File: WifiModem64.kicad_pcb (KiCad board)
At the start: 2 copper layers, 55.9 x 59.7 mm, 39 parts, among them J1 C64-UserPort, J2 USB_B, Q1 BSS138, Q2 BSS138, Q3 BSS138, Q4 BSS138, SW1 Push, SW2 Reset, U1 WeMos_mini, U2 WeMos_D1_mini_OLED_Shield

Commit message: Added pull-down resistor on GPIO15 that is needed for internal flash boot.
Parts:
- added R9: 3k3, Resistors_SMD:R_0805_HandSoldering, B.Cu at (146.7, 108.6)
- moved REF** 1.91 mm to (147.3, 106.0)
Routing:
- net W_D8: track 51.7 -> 58.4 mm
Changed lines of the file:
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@@
 (kicad_pcb (version 4) (host pcbnew 4.0.7)
   (general
-    (links 86)
+    (links 88)
     (no_connects 0)
-    (area 118.644999 52.545 177.408 134.275001)
+    (area 118.669999 67.869999 174.700001 127.710001)
     (thickness 1.6)
     (drawings 47)
-    (tracks 272)
+    (tracks 276)
     (zones 0)
-    (modules 39)
+    (modules 40)
     (nets 39)
   )
@@
   )
   (module hackup:VIA-0.6mm (layer F.Cu)
-    (at 147.32 107.95)
+    (at 147.32 106.045)
     (fp_text reference REF** (at 0 1.2) (layer F.SilkS) hide
       (effects (font (size 1 1) (thickness 0.15)))
@@
     )
   )
+  (module Resistors_SMD:R_0805_HandSoldering (layer B.Cu)
+    (at 146.685 108.585 180)
+    (descr "Resistor SMD 0805, hand soldering")
+    (tags "resistor 0805")
+    (attr smd)
+    (fp_text reference R9 (at 0 1.7 180) (layer B.SilkS)
+      (effects (font (size 1 1) (thickness 0.15)) (justify mirror))
+    )
+    (fp_text value 3k3 (at 0 -1.75 180) (layer B.Fab)
+      (effects (font (size 1 1) (thickness 0.15)) (justify mirror))
+    )
+    (fp_text user %R (at 0 0 180) (layer B.Fab)
+      (effects (font (size 0.5 0.5) (thickness 0.075)) (justify mirror))
+    )
+    (fp_line (start -1 -0.62) (end -1 0.62) (layer B.Fab) (width 0.1))
+    (fp_line (start 1 -0.62) (end -1 -0.62) (layer B.Fab) (width 0.1))
+    (fp_line (start 1 0.62) (end 1 -0.62) (layer B.Fab) (width 0.1))
+    (fp_line (start -1 0.62) (end 1 0.62) (layer B.Fab) (width 0.1))
+    (fp_line (start 0.6 -0.88) (end -0.6 -0.88) (layer B.SilkS) (width 0.12))
+    (fp_line (start -0.6 0.88) (end 0.6 0.88) (layer B.SilkS) (width 0.12))
+    (fp_line (start -2.35 0.9) (end 2.35 0.9) (layer B.CrtYd) (width 0.05))
+    (fp_line (start -2.35 0.9) (end -2.35 -0.9) (layer B.CrtYd) (width 0.05))
+    (fp_line (start 2.35 -0.9) (end 2.35 0.9) (layer B.CrtYd) (width 0.05))
+    (fp_line (start 2.35 -0.9) (end -2.35 -0.9) (layer B.CrtYd) (width 0.05))
+    (pad 1 smd rect (at -1.35 0 180) (size 1.5 1.3) (layers B.Cu B.Paste B.Mask)
+      (net 25 GND))
+    (pad 2 smd rect (at 1.35 0 180) (size 1.5 1.3) (layers B.Cu B.Paste B.Mask)
+      (net 18 W_D8))
+    (model ${KISYS3DMOD}/Resistors_SMD.3dshapes/R_0805.wrl
+      (at (xyz 0 0 0))
+      (scale (xyz 1 1 1))
+      (rotate (xyz 0 0 0))
+    )
+  )
   (dimension 59.69 (width 0.3) (layer Dwgs.User)
     (gr_text "59.690 mm" (at 196.803 97.79 90) (layer Dwgs.User)
@@
   (segment (start 148.546411 99.015001) (end 170.859999 99.015001) (width 0.25) (layer F.Cu) (net 17))
   (segment (start 143.51 97.79) (end 147.32141 97.79) (width 0.25) (layer F.Cu) (net 17))
+  (segment (start 141.732 113.204) (end 142.632 113.204) (width 0.25) (layer B.Cu) (net 18))
+  (segment (start 142.632 113.204) (end 145.335 110.501) (width 0.25) (layer B.Cu) (net 18))
+  (segment (start 145.335 110.501) (end 145.335 109.485) (width 0.25) (layer B.Cu) (net 18))
+  (segment (start 145.335 109.485) (end 145.335 108.585) (width 0.25) (layer B.Cu) (net 18))
   (segment (start 141.732 113.204) (end 141.732 107.823) (width 0.25) (layer B.Cu) (net 18))
   (segment (start 141.732 107.823) (end 149.225 100.33) (width 0.25) (layer B.Cu) (net 18))

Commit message: Pull down resistor is not optional so it should be through hole.
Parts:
- R9: footprint Resistors_SMD:R_0805_HandSoldering -> Resistors_THT:R_Axial_DIN0207_L6.3mm_D2.5mm_P2.54mm_Vertical; moved to F.Cu
- moved R9 25.9 mm to (121.9, 116.2), turned to 90 degrees
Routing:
- net W_D8: track 58.4 -> 65.6 mm
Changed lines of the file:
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@@
     (thickness 1.6)
     (drawings 47)
-    (tracks 276)
+    (tracks 274)
     (zones 0)
     (modules 40)
@@
   )
   (layers
-    (0 F.Cu signal hide)
+    (0 F.Cu signal)
     (31 B.Cu signal)
     (32 B.Adhes user)
@@
     )
   )
-  (module Resistors_SMD:R_0805_HandSoldering (layer B.Cu)
-    (at 146.685 108.585 180)
-    (descr "Resistor SMD 0805, hand soldering")
-    (tags "resistor 0805")
-    (attr smd)
-    (fp_text reference R9 (at 0 1.7 180) (layer B.SilkS)
-      (effects (font (size 1 1) (thickness 0.15)) (justify mirror))
-    )
-    (fp_text value 3k3 (at 0 -1.75 180) (layer B.Fab)
-      (effects (font (size 1 1) (thickness 0.15)) (justify mirror))
-    )
-    (fp_text user %R (at 0 0 180) (layer B.Fab)
-      (effects (font (size 0.5 0.5) (thickness 0.075)) (justify mirror))
-    )
-    (fp_line (start -1 -0.62) (end -1 0.62) (layer B.Fab) (width 0.1))
-    (fp_line (start 1 -0.62) (end -1 -0.62) (layer B.Fab) (width 0.1))
-    (fp_line (start 1 0.62) (end 1 -0.62) (layer B.Fab) (width 0.1))
-    (fp_line (start -1 0.62) (end 1 0.62) (layer B.Fab) (width 0.1))
-    (fp_line (start 0.6 -0.88) (end -0.6 -0.88) (layer B.SilkS) (width 0.12))
-    (fp_line (start -0.6 0.88) (end 0.6 0.88) (layer B.SilkS) (width 0.12))
-    (fp_line (start -2.35 0.9) (end 2.35 0.9) (layer B.CrtYd) (width 0.05))
-    (fp_line (start -2.35 0.9) (end -2.35 -0.9) (layer B.CrtYd) (width 0.05))
-    (fp_line (start 2.35 -0.9) (end 2.35 0.9) (layer B.CrtYd) (width 0.05))
-    (fp_line (start 2.35 -0.9) (end -2.35 -0.9) (layer B.CrtYd) (width 0.05))
-    (pad 1 smd rect (at -1.35 0 180) (size 1.5 1.3) (layers B.Cu B.Paste B.Mask)
+  (module Resistors_THT:R_Axial_DIN0207_L6.3mm_D2.5mm_P2.54mm_Vertical (layer F.Cu)
+    (at 121.92 116.205 90)
+    (descr "Resistor, Axial_DIN0207 series, Axial, Vertical, pin pitch=2.54mm, 0.25W = 1/4W, length*diameter=6.3*2.5mm^2, http://cdn-reichelt.de/documents/datenblatt/B400/1_4W%23YAG.pdf")
+    (tags "Resistor Axial_DIN0207 series Axial Vertical pin pitch 2.54mm 0.25W = 1/4W length 6.3mm diameter 2.5mm")
+    (fp_text reference R9 (at 1.27 -2.31 90) (layer F.SilkS)
+      (effects (font (size 1 1) (thickness 0.15)))
+    )
+    (fp_text value 3k3 (at 1.27 2.31 90) (layer F.Fab)
+      (effects (font (size 1 1) (thickness 0.15)))
+    )
+    (fp_circle (center 0 0) (end 1.25 0) (layer F.Fab) (width 0.1))
+    (fp_circle (center 0 0) (end 1.31 0) (layer F.SilkS) (width 0.12))
+    (fp_line (start 0 0) (end 2.54 0) (layer F.Fab) (width 0.1))
+    (fp_line (start 1.31 0) (end 1.44 0) (layer F.SilkS) (width 0.12))
+    (fp_line (start -1.6 -1.6) (end -1.6 1.6) (layer F.CrtYd) (width 0.05))
+    (fp_line (start -1.6 1.6) (end 3.65 1.6) (layer F.CrtYd) (width 0.05))
+    (fp_line (start 3.65 1.6) (end 3.65 -1.6) (layer F.CrtYd) (width 0.05))
+    (fp_line (start 3.65 -1.6) (end -1.6 -1.6) (layer F.CrtYd) (width 0.05))
+    (pad 1 thru_hole circle (at 0 0 90) (size 1.6 1.6) (drill 0.8) (layers *.Cu *.Mask)
       (net 25 GND))
-    (pad 2 smd rect (at 1.35 0 180) (size 1.5 1.3) (layers B.Cu B.Paste B.Mask)
+    (pad 2 thru_hole oval (at 2.54 0 90) (size 1.6 1.6) (drill 0.8) (layers *.Cu *.Mask)
       (net 18 W_D8))
-    (model ${KISYS3DMOD}/Resistors_SMD.3dshapes/R_0805.wrl
-      (at (xyz 0 0 0))
-      (scale (xyz 1 1 1))
+    (model ${KISYS3DMOD}/Resistors_THT.3dshapes/R_Axial_DIN0207_L6.3mm_D2.5mm_P2.54mm_Vertical.wrl
+      (at (xyz 0 0 0))
+      (scale (xyz 0.393701 0.393701 0.393701))
       (rotate (xyz 0 0 0))
     )
@@
   (segment (start 148.546411 99.015001) (end 170.859999 99.015001) (width 0.25) (layer F.Cu) (net 17))
   (segment (start 143.51 97.79) (end 147.32141 97.79) (width 0.25) (layer F.Cu) (net 17))
-  (segment (start 141.732 113.204) (end 142.632 113.204) (width 0.25) (layer B.Cu) (net 18))
-  (segment (start 142.632 113.204) (end 145.335 110.501) (width 0.25) (layer B.Cu) (net 18))
-  (segment (start 145.335 110.501) (end 145.335 109.485) (width 0.25) (layer B.Cu) (net 18))
-  (segment (start 145.335 109.485) (end 145.335 108.585) (width 0.25) (layer B.Cu) (net 18))
+  (segment (start 120.65 100.33) (end 121.92 101.6) (width 0.25) (layer B.Cu) (net 18))
+  (segment (start 121.92 101.6) (end 121.92 113.665) (width 0.25) (layer B.Cu) (net 18))
   (segment (start 141.732 113.204) (end 141.732 107.823) (width 0.25) (layer B.Cu) (net 18))
   (segment (start 141.732 107.823) (end 149.225 100.33) (width 0.25) (layer B.Cu) (net 18))

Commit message: Upgraded project files, modfied resistor footprint.
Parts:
- R9: footprint Resistors_THT:R_Axial_DIN0207_L6.3mm_D2.5mm_P2.54mm_Vertical -> Resistors_THT:R_Axial_DIN0207_L6.3mm_D2.5mm_P7.62mm_Horizontal
- moved R9 1.42 mm to (123.2, 115.6)
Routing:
- net W_D8: track 65.6 -> 60.4 mm
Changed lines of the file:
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@@
-(kicad_pcb (version 4) (host pcbnew 4.0.7)
+(kicad_pcb (version 20171130) (host pcbnew "(2017-12-18 revision 3c6d17026)-makepkg")
   (general
-    (links 88)
-    (no_connects 0)
-    (area 118.669999 67.869999 174.700001 127.710001)
     (thickness 1.6)
     (drawings 47)
@@
     (aux_axis_origin 118.745 67.945)
     (grid_origin 118.745 67.945)
-    (visible_elements 7FFEFFFF)
+    (visible_elements 7FFFFFFF)
     (pcbplotparams
       (layerselection 0x010f0_80000001)
       (usegerberextensions true)
+      (usegerberattributes false)
+      (usegerberadvancedattributes false)
+      (creategerberjobfile false)
       (excludeedgelayer true)
       (linewidth 0.100000)
@@
       (hpglpenspeed 20)
       (hpglpendiameter 15)
-      (hpglpenoverlay 2)
       (psnegative false)
       (psa4output false)
@@
       (effects (font (size 1 1) (thickness 0.15)) (justify mirror))
     )
-    (fp_text user %R (at 0 0 360) (layer B.Fab)
+    (fp_text user %R (at 0 0) (layer B.Fab)
       (effects (font (size 0.5 0.5) (thickness 0.075)) (justify mirror))
     )
@@
       (effects (font (size 1 1) (thickness 0.15)) (justify mirror))
     )
-    (fp_text user %R (at 0 0 360) (layer B.Fab)
+    (fp_text user %R (at 0 0) (layer B.Fab)
       (effects (font (size 0.5 0.5) (thickness 0.075)) (justify mirror))
     )
@@
       (effects (font (size 1 1) (thickness 0.15)) (justify mirror))
     )
-    (fp_text user %R (at 0 0 360) (layer B.Fab)
+    (fp_text user %R (at 0 0) (layer B.Fab)
       (effects (font (size 0.5 0.5) (thickness 0.075)) (justify mirror))
     )
@@
       (effects (font (size 1 1) (thickness 0.15)) (justify mirror))
     )
-    (fp_text user %R (at 0 0 360) (layer B.Fab)
+    (fp_text user %R (at 0 0) (layer B.Fab)
       (effects (font (size 0.5 0.5) (thickness 0.075)) (justify mirror))
     )
@@
     (tags "solder bridge")
     (attr smd)
-    (fp_text reference JP1 (at -1.778 -0.0635 450) (layer B.SilkS)
-      (effects (font (size 1 1) (thickness 0.15)) (justify mirror))
-    )
-    (fp_text value PwrSafety (at -1.8 0 450) (layer B.Fab)
+    (fp_text reference JP1 (at -1.778 -0.0635 90) (layer B.SilkS)
+      (effects (font (size 1 1) (thickness 0.15)) (justify mirror))
+    )
+    (fp_text value PwrSafety (at -1.8 0 90) (layer B.Fab)
       (effects (font (size 1 1) (thickness 0.15)) (justify mirror))
     )
@@
     )
   )
-  (module Resistors_THT:R_Axial_DIN0207_L6.3mm_D2.5mm_P2.54mm_Vertical (layer F.Cu)
-    (at 121.92 116.205 90)
-    (descr "Resistor, Axial_DIN0207 series, Axial, Vertical, pin pitch=2.54mm, 0.25W = 1/4W, length*diameter=6.3*2.5mm^2, http://cdn-reichelt.de/documents/datenblatt/B400/1_4W%23YAG.pdf")
-    (tags "Resistor Axial_DIN0207 series Axial Vertical pin pitch 2.54mm 0.25W = 1/4W length 6.3mm diameter 2.5mm")
-    (fp_text reference R9 (at 1.27 -2.31 90) (layer F.SilkS)
-      (effects (font (size 1 1) (thickness 0.15)))
-    )
-    (fp_text value 3k3 (at 1.27 2.31 90) (layer F.Fab)
-      (effects (font (size 1 1) (thickness 0.15)))
-    )
-    (fp_circle (center 0 0) (end 1.25 0) (layer F.Fab) (width 0.1))
-    (fp_circle (center 0 0) (end 1.31 0) (layer F.SilkS) (width 0.12))
-    (fp_line (start 0 0) (end 2.54 0) (layer F.Fab) (width 0.1))
-    (fp_line (start 1.31 0) (end 1.44 0) (layer F.SilkS) (width 0.12))
-    (fp_line (start -1.6 -1.6) (end -1.6 1.6) (layer F.CrtYd) (width 0.05))
-    (fp_line (start -1.6 1.6) (end 3.65 1.6) (layer F.CrtYd) (width 0.05))
-    (fp_line (start 3.65 1.6) (end 3.65 -1.6) (layer F.CrtYd) (width 0.05))
-    (fp_line (start 3.65 -1.6) (end -1.6 -1.6) (layer F.CrtYd) (width 0.05))
+  (module Resistors_THT:R_Axial_DIN0207_L6.3mm_D2.5mm_P7.62mm_Horizontal (layer F.Cu)
+    (at 123.19 115.57 90)
+    (descr "Resistor, Axial_DIN0207 series, Axial, Horizontal, pin pitch=7.62mm, 0.25W = 1/4W, length*diameter=6.3*2.5mm^2, http://cdn-reichelt.de/documents/datenblatt/B400/1_4W%23YAG.pdf")
+    (tags "Resistor Axial_DIN0207 series Axial Horizontal pin pitch 7.62mm 0.25W = 1/4W length 6.3mm diameter 2.5mm")
+    (fp_text reference R9 (at 3.81 -2.31 90) (layer F.SilkS)
+      (effects (font (size 1 1) (thickness 0.15)))
+    )
+    (fp_text value 3k3 (at 3.81 2.31 90) (layer F.Fab)
+      (effects (font (size 1 1) (thickness 0.15)))
+    )
+    (fp_line (start 0.66 -1.25) (end 0.66 1.25) (layer F.Fab) (width 0.1))
+    (fp_line (start 0.66 1.25) (end 6.96 1.25) (layer F.Fab) (width 0.1))
+    (fp_line (start 6.96 1.25) (end 6.96 -1.25) (layer F.Fab) (width 0.1))
+    (fp_line (start 6.96 -1.25) (end 0.66 -1.25) (layer F.Fab) (width 0.1))
+    (fp_line (start 0 0) (end 0.66 0) (layer F.Fab) (width 0.1))
+    (fp_line (start 7.62 0) (end 6.96 0) (layer F.Fab) (width 0.1))
+    (fp_line (start 0.6 -0.98) (end 0.6 -1.31) (layer F.SilkS) (width 0.12))
+    (fp_line (start 0.6 -1.31) (end 7.02 -1.31) (layer F.SilkS) (width 0.12))
+    (fp_line (start 7.02 -1.31) (end 7.02 -0.98) (layer F.SilkS) (width 0.12))
+    (fp_line (start 0.6 0.98) (end 0.6 1.31) (layer F.SilkS) (width 0.12))
+    (fp_line (start 0.6 1.31) (end 7.02 1.31) (layer F.SilkS) (width 0.12))
+    (fp_line (start 7.02 1.31) (end 7.02 0.98) (layer F.SilkS) (width 0.12))
+    (fp_line (start -1.05 -1.6) (end -1.05 1.6) (layer F.CrtYd) (width 0.05))
+    (fp_line (start -1.05 1.6) (end 8.7 1.6) (layer F.CrtYd) (width 0.05))
+    (fp_line (start 8.7 1.6) (end 8.7 -1.6) (layer F.CrtYd) (width 0.05))
+    (fp_line (start 8.7 -1.6) (end -1.05 -1.6) (layer F.CrtYd) (width 0.05))
     (pad 1 thru_hole circle (at 0 0 90) (size 1.6 1.6) (drill 0.8) (layers *.Cu *.Mask)
       (net 25 GND))
-    (pad 2 thru_hole oval (at 2.54 0 90) (size 1.6 1.6) (drill 0.8) (layers *.Cu *.Mask)
+    (pad 2 thru_hole oval (at 7.62 0 90) (size 1.6 1.6) (drill 0.8) (layers *.Cu *.Mask)
       (net 18 W_D8))
-    (model ${KISYS3DMOD}/Resistors_THT.3dshapes/R_Axial_DIN0207_L6.3mm_D2.5mm_P2.54mm_Vertical.wrl
+    (model ${KISYS3DMOD}/Resistors_THT.3dshapes/R_Axial_DIN0207_L6.3mm_D2.5mm_P7.62mm_Horizontal.wrl
       (at (xyz 0 0 0))
       (scale (xyz 0.393701 0.393701 0.393701))
@@
   (segment (start 148.546411 99.015001) (end 170.859999 99.015001) (width 0.25) (layer F.Cu) (net 17))
   (segment (start 143.51 97.79) (end 147.32141 97.79) (width 0.25) (layer F.Cu) (net 17))
-  (segment (start 120.65 100.33) (end 121.92 101.6) (width 0.25) (layer B.Cu) (net 18))
-  (segment (start 121.92 101.6) (end 121.92 113.665) (width 0.25) (layer B.Cu) (net 18))
+  (segment (start 123.19 107.95) (end 123.19 102.87) (width 0.25) (layer B.Cu) (net 18))
+  (segment (start 123.19 102.87) (end 120.65 100.33) (width 0.25) (layer B.Cu) (net 18))
   (segment (start 141.732 113.204) (end 141.732 107.823) (width 0.25) (layer B.Cu) (net 18))
   (segment (start 141.732 107.823) (end 149.225 100.33) (width 0.25) (layer B.Cu) (net 18))

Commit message: Freed GPIO15 and fixed footprints.
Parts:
- removed R9: 3k3, Resistors_THT:R_Axial_DIN0207_L6.3mm_D2.5mm_P7.62mm_Horizontal
- D1: footprint Diodes_SMD:D_0805 -> Diodes_SMD:D_SOD-323_HandSoldering
- Q1, Q2, Q3, Q4: footprint TO_SOT_Packages_SMD:SOT-23 -> TO_SOT_Packages_SMD:SOT-23_Handsoldering
- moved Q4 0.89 mm to (166.9, 108.5)
- moved Q1 0.89 mm to (158.6, 113.2)
- moved Q2 0.89 mm to (138.9, 113.2)
- moved Q3 0.89 mm to (130.7, 108.5)
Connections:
- JP3 pad 2: W_D8 -> W_D7
- Q2 pad 3: W_D8 -> W_D7
- R6 pad 2: W_D8 -> W_D7
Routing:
- net W_D8: track 60.4 -> 29.6 mm
- net W_D7: track 29.6 -> 55.7 mm
- net +3V3: track 99.9 -> 102.0 mm
- net RTS: track 12.0 -> 13.6 mm
- net W_D6: track 56.6 -> 58.1 mm
- net W_RX: track 60.8 -> 62.3 mm
- net W_TX: track 60.4 -> 61.9 mm
- net SP2: track 43.9 -> 45.4 mm
- net CTS: track 11.8 -> 13.2 mm
- net SP1: track 47.9 -> 49.3 mm

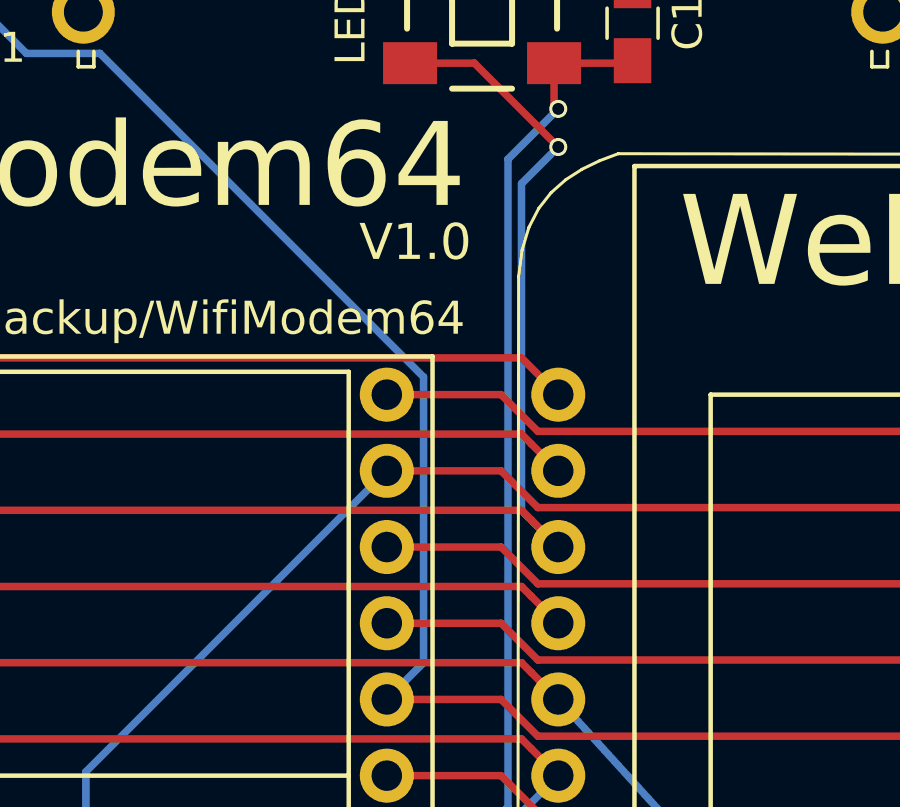
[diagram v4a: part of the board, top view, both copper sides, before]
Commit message: WS2812b not working on D0.
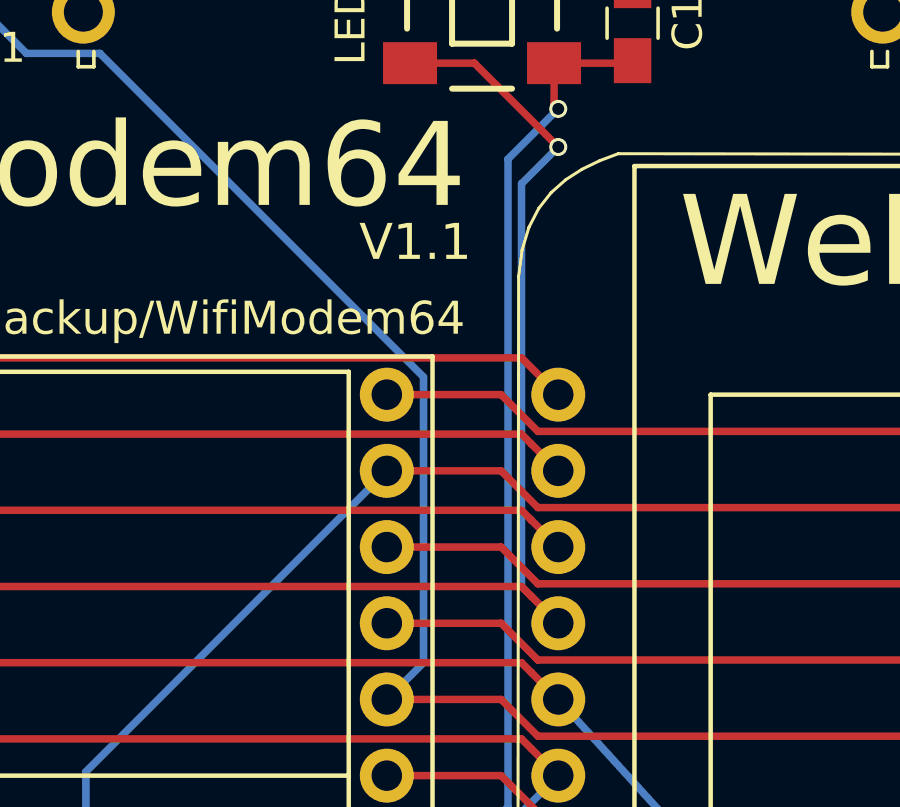
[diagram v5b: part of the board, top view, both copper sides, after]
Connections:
- LED1 pad 4: W_D0 -> W_D5
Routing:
- net W_D5: track 29.6 -> 52.8 mm, vias 0 -> 1
- net W_D0: track 50.2 -> 29.6 mm, vias 1 -> 0
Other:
- board text added: "V1.1"
- board text removed: "V1.0"
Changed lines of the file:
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@@
       (net 25 GND))
     (pad 4 smd rect (at 1.65 2.4 270) (size 1.4 1.8) (layers F.Cu F.Paste F.Mask)
-      (net 22 W_D0))
+      (net 21 W_D5))
   )
   (module Capacitors_SMD:C_0805_HandSoldering (layer F.Cu)
@@
     (effects (font (size 1.1 1.1) (thickness 0.2)))
   )
-  (gr_text V1.0 (at 144.4625 80.01) (layer F.SilkS)
+  (gr_text V1.1 (at 144.4625 80.01) (layer F.SilkS)
     (effects (font (size 1.2 1.2) (thickness 0.2)))
   )
@@
   (segment (start 155.575 102.235) (end 149.225 95.25) (width 0.25) (layer B.Cu) (net 20) (status 20))
   (segment (start 161.259 113.046) (end 161.417 113.204) (width 0.25) (layer B.Cu) (net 20))
+  (segment (start 149.225 76.835) (end 147.999999 78.060001) (width 0.25) (layer B.Cu) (net 21))
+  (segment (start 147.999999 78.060001) (end 147.999999 91.484999) (width 0.25) (layer B.Cu) (net 21))
+  (segment (start 147.999999 91.484999) (end 148.325001 91.810001) (width 0.25) (layer B.Cu) (net 21))
+  (segment (start 148.325001 91.810001) (end 149.225 92.71) (width 0.25) (layer B.Cu) (net 21))
   (segment (start 120.65 92.71) (end 121.875001 91.484999) (width 0.25) (layer F.Cu) (net 21))
   (segment (start 121.875001 91.484999) (end 147.999999 91.484999) (width 0.25) (layer F.Cu) (net 21))
   (segment (start 147.999999 91.484999) (end 148.325001 91.810001) (width 0.25) (layer F.Cu) (net 21))
   (segment (start 148.325001 91.810001) (end 149.225 92.71) (width 0.25) (layer F.Cu) (net 21))
-  (segment (start 147.999999 78.060001) (end 147.999999 88.944999) (width 0.25) (layer B.Cu) (net 22))
-  (segment (start 149.225 76.835) (end 147.999999 78.060001) (width 0.25) (layer B.Cu) (net 22))
-  (segment (start 147.999999 88.944999) (end 148.325001 89.270001) (width 0.25) (layer B.Cu) (net 22))
-  (segment (start 148.325001 89.270001) (end 149.225 90.17) (width 0.25) (layer B.Cu) (net 22))
-  (segment (start 144.285 74.04) (end 146.43 74.04) (width 0.25) (layer F.Cu) (net 22))
-  (segment (start 146.43 74.04) (end 149.225 76.835) (width 0.25) (layer F.Cu) (net 22))
-  (via (at 149.225 76.835) (size 0.6) (drill 0.4) (layers F.Cu B.Cu) (net 22))
-  (segment (start 144.145 74.18) (end 144.285 74.04) (width 0.25) (layer F.Cu) (net 22))
+  (segment (start 144.145 74.18) (end 144.285 74.04) (width 0.25) (layer F.Cu) (net 21))
+  (segment (start 146.43 74.04) (end 149.225 76.835) (width 0.25) (layer F.Cu) (net 21))
+  (segment (start 147.999999 88.944999) (end 148.325001 89.270001) (width 0.25) (layer F.Cu) (net 22))
+  (segment (start 144.285 74.04) (end 146.43 74.04) (width 0.25) (layer F.Cu) (net 21))
+  (via (at 149.225 76.835) (size 0.6) (drill 0.4) (layers F.Cu B.Cu) (net 21))
   (segment (start 120.65 90.17) (end 121.875001 88.944999) (width 0.25) (layer F.Cu) (net 22))
   (segment (start 121.875001 88.944999) (end 147.999999 88.944999) (width 0.25) (layer F.Cu) (net 22))
-  (segment (start 147.999999 88.944999) (end 148.325001 89.270001) (width 0.25) (layer F.Cu) (net 22))
   (segment (start 148.325001 89.270001) (end 149.225 90.17) (width 0.25) (layer F.Cu) (net 22))
   (segment (start 120.65 87.63) (end 121.875001 86.404999) (width 0.25) (layer F.Cu) (net 23))
